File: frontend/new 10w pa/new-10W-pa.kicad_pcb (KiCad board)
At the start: 2 copper layers, 100 x 100 mm, 169 parts, among them K1 D3002, K2 D3002, K3 D3002, K4 D3002, K5 D3002, K6 D3002, P1 CONN_01X02, P2 CONN_02X01, P3 From HL CN3, P4 CONN_01X02, P5 CONN_01X02, P6 CONN_01X01, P7 From FE CN2, P8 CONN_01X08, P9 CONN_02X05, Q1 2N3906, Q3 RD16HHF1, T1 TRANSFO, T2 OUT_TRANSF, U1 74HC14, U2 74HC14, U3 TPIC6B595, U4 TPIC6B595, U5 TPIC6B595, U6 TPIC6B595, U7 LP2951-50D

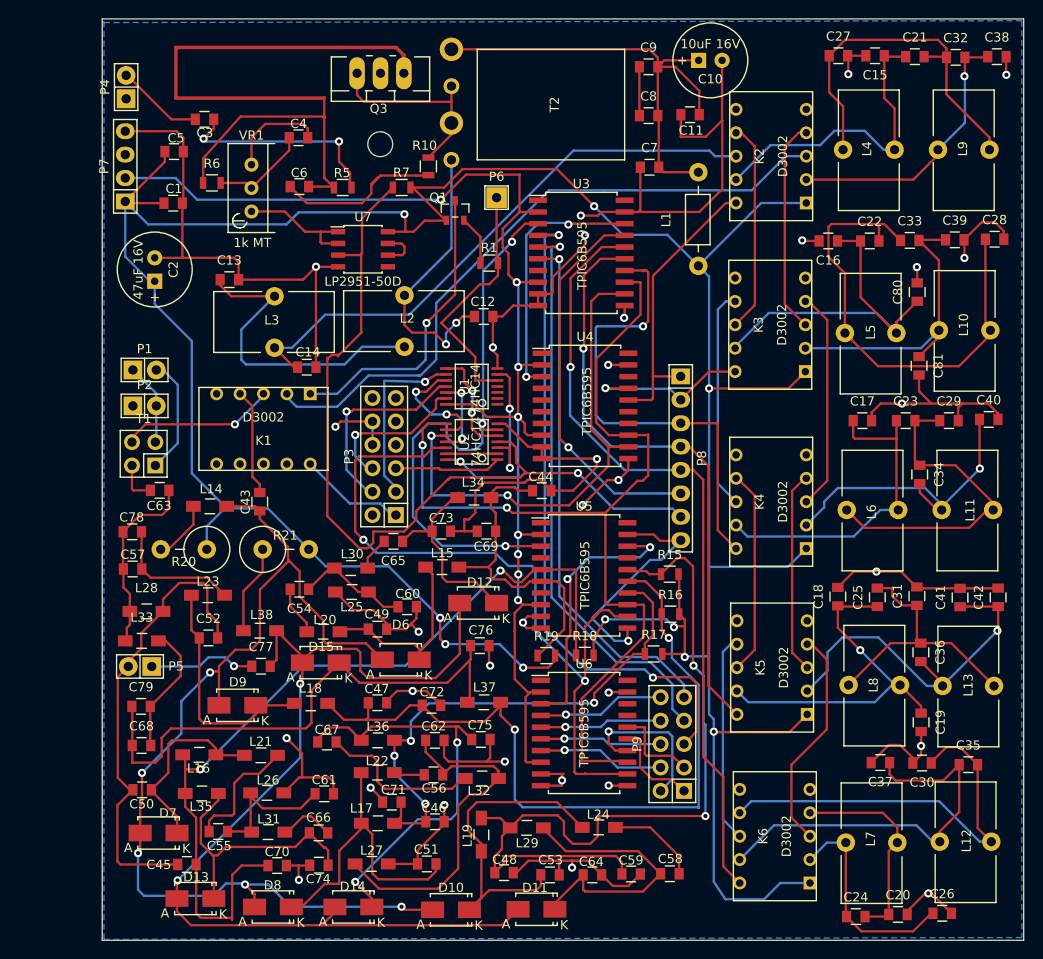
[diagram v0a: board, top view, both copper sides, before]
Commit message: new superband design and updated pcb
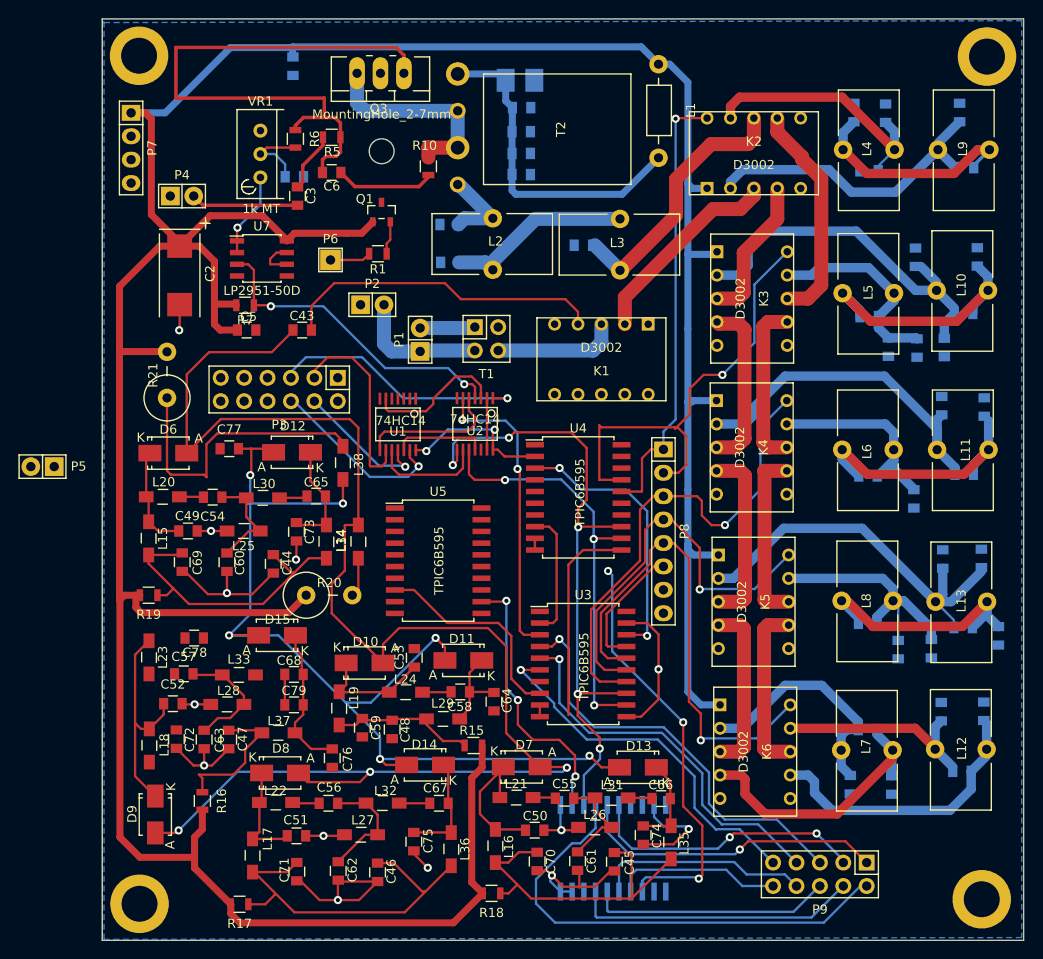
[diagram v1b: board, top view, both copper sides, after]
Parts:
- added MH: VAL**, HERMESLITE:MH, F.Cu at (196.0, 54.1)
- added MH: VAL**, HERMESLITE:MH, F.Cu at (195.5, 145.5)
- added MH: VAL**, HERMESLITE:MH, F.Cu at (104.0, 54.0)
- added MH: VAL**, HERMESLITE:MH, F.Cu at (104.1, 146.0)
- C1, C11, C12, C13, C14, C15, C16, C17, C18, C19, C20, C21, C22, C23, C24, C25, C26, C27, C28, C29, C30, C31, C32, C33, C34, C35, C36, C37, C38, C39, C4, C40, C41, C42, C7, C8, C80, C81, C9, U6: moved to B.Cu
- C10: footprint Discret:C1V8 -> Capacitors_Tantalum_SMD:TantalC_SizeB_EIA-3528_Reflow; moved to B.Cu
- C2: footprint Discret:C1V8 -> Capacitors_Tantalum_SMD:TantalC_SizeD_EIA-7343_Reflow
- moved R16 54.7 mm to (110.9, 134.9), turned to 270 degrees
- moved R17 52.5 mm to (114.9, 146.1), turned to 180 degrees
- moved L35 51.2 mm to (161.7, 139.4), turned to 270 degrees
- moved D13 50.1 mm to (158.1, 131.2)
- moved C45 46.4 mm to (155.6, 141.5), turned to 270 degrees
- moved U3 44.6 mm to (152.2, 120.0)
- moved R19 43.7 mm to (105.0, 112.5), turned to 180 degrees
- moved C50 42.8 mm to (146.9, 138.0), turned to 0 degrees
- moved D7 40.1 mm to (145.5, 131.2), turned to 180 degrees
- moved T1 39.2 mm to (141.7, 84.7), turned to 180 degrees
- moved L3 38.4 mm to (149.6, 77.8)
- moved C55 37.8 mm to (150.2, 134.6)
- moved K1 37.4 mm to (154.2, 86.9)
- moved L31 37.4 mm to (155.3, 134.5)
- moved C66 37.4 mm to (160.7, 134.6), turned to 180 degrees
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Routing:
- net GND: track 456.1 -> 132.0 mm, vias 33 -> 13
- net +5V: track 147.3 -> 54.0 mm, vias 9 -> 2
- net Net-(C48-Pad1): track 88.2 -> 15.6 mm, vias 2 -> 0
- net Net-(C47-Pad1): track 84.4 -> 15.3 mm, vias 2 -> 0
- net /PTT: track 94.1 -> 34.8 mm, vias 1 -> 2
- net Net-(C45-Pad1): track 92.9 -> 37.2 mm, vias 2 -> 0
- net RX-Load: track 81.5 -> 29.8 mm, vias 2 -> 3
- net Net-(C43-Pad1): track 112.6 -> 163.4 mm, vias 5 -> 3
- net TXOUT: track 72.0 -> 22.3 mm
- net Net-(C68-Pad1): track 58.7 -> 16.1 mm
- net SPI-CLK: track 106.2 -> 70.9 mm, vias 2 -> 5
- net Net-(P9-Pad2): track 17.3 -> 52.3 mm, vias 1 -> 0
- net Net-(C67-Pad1): track 46.7 -> 11.8 mm, vias 2 -> 0
- net +12V: track 338.3 -> 372.7 mm, vias 10 -> 0
- net TXIN: track 62.6 -> 29.1 mm
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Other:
- net class Power added: clearance 0.254, trace_width 0.762, via_dia 0.889, via_drill 0.635
- net class RF added: clearance 0.508, trace_width 1.524, via_dia 0.889, via_drill 0.635
- net class RF-N added: clearance 0.254, trace_width 1.016, via_dia 0.889, via_drill 0.635

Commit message: Board files updated
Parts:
- added MH: VAL**, HERMESLITE:MH, F.Cu at (146.2, 54.1)
- added MH: VAL**, HERMESLITE:MH, F.Cu at (104.0, 96.1)
- added MH: VAL**, HERMESLITE:MH, F.Cu at (146.1, 84.6)
- moved P5 20.6 mm to (103.0, 80.3), turned to 90 degrees
- moved P2 11.2 mm to (125.6, 70.4)
- moved C11 9.17 mm to (153.8, 63.1), turned to 90 degrees
- moved C10 7.27 mm to (143.7, 63.7), turned to 270 degrees
- moved C8 6.30 mm to (151.6, 63.0), turned to 90 degrees
- moved P1 5.78 mm to (130.6, 80.5)
- moved R17 5.52 mm to (113.1, 140.9)
- moved T1 5.09 mm to (137.2, 82.4)
- moved C9 3.91 mm to (149.3, 63.0), turned to 90 degrees
- moved C7 3.66 mm to (147.0, 63.0), turned to 90 degrees
- moved D6 2.56 mm to (109.7, 96.5), turned to 270 degrees
- moved K1 2.26 mm to (156.4, 87.3), turned to 270 degrees
- moved R21 1.42 mm to (106.2, 87.5)
- moved L36 0.65 mm to (137.3, 139.8)
- moved C62 0.05 mm to (125.6, 142.5)
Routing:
- net +5V: track 54.0 -> 224.1 mm, vias 2 -> 12
- net GND: track 132.0 -> 266.7 mm, vias 13 -> 32
- net Net-(C47-Pad1): track 15.3 -> 74.3 mm, vias 0 -> 2
- net Net-(C45-Pad1): track 37.2 -> 78.4 mm, vias 0 -> 2
- net /PTT: track 34.8 -> 74.4 mm, vias 2 -> 6
- net Net-(K1-Pad1): track 0.00 -> 31.0 mm
- net Net-(C46-Pad1): track 40.5 -> 67.7 mm, vias 0 -> 2
- net Net-(C48-Pad1): track 15.6 -> 41.5 mm, vias 0 -> 3
- net RX-OUT: track 0.00 -> 20.6 mm, vias 0 -> 2
- net SPI-DATA: track 32.9 -> 51.0 mm, vias 2 -> 4
- net Net-(P6-Pad1): track 4.47 -> 22.4 mm, vias 0 -> 1
- net RX-Load: track 29.8 -> 47.4 mm, vias 3 -> 4
- net Net-(U5-Pad18): track 45.4 -> 62.6 mm, vias 3 -> 5
- net Net-(P9-Pad2): track 52.3 -> 41.1 mm, vias 0 -> 1
- net SPI-CLK: track 70.9 -> 81.4 mm, vias 5 -> 6
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
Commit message: Upload latest pcb changes
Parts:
- removed MH (x7): VAL**, HERMESLITE:MH
- removed MountingHole_2-7mm: VAL**, Mounting_Holes:MountingHole_2-7mm
- added MountingHole_4mm: VAL**, Mounting_Holes:MountingHole_4mm, F.Cu at (104.4, 92.4)
- added MountingHole_4mm: VAL**, Mounting_Holes:MountingHole_4mm, F.Cu at (146.4, 84.1)
- added MountingHole_4mm: VAL**, Mounting_Holes:MountingHole_4mm, F.Cu at (146.6, 53.8)
- added MountingHole_4mm: VAL**, Mounting_Holes:MountingHole_4mm, F.Cu at (104.3, 54.3)
- added MountingHole_4mm: VAL**, Mounting_Holes:MountingHole_4mm, F.Cu at (104.2, 145.8)
- added MountingHole_4mm: VAL**, Mounting_Holes:MountingHole_4mm, F.Cu at (195.6, 145.7)
- added MountingHole_4mm: VAL**, Mounting_Holes:MountingHole_4mm, F.Cu at (195.6, 54.3)
- added MountingHole_6mm: VAL**, Mounting_Holes:MountingHole_6mm, F.Cu at (130.5, 66.9)
- U6: moved to F.Cu
- moved C45 47.9 mm to (115.9, 114.6), turned to 0 degrees
- moved C50 40.7 mm to (115.7, 112.0)
- moved C66 40.6 mm to (128.9, 109.4)
- moved C74 40.3 mm to (128.8, 111.6), turned to 180 degrees
- moved D7 40.0 mm to (108.6, 115.9), turned to 90 degrees
- moved L31 39.9 mm to (124.2, 109.5)
- moved L16 39.7 mm to (112.7, 113.8)
- moved C55 39.6 mm to (119.4, 109.6)
- moved C61 39.5 mm to (124.5, 112.6)
- moved L26 39.4 mm to (122.4, 113.6), turned to 270 degrees
- moved L35 39.3 mm to (132.1, 113.6)
- moved L21 39.3 mm to (114.5, 109.7)
- moved R18 36.4 mm to (119.7, 116.3), turned to 90 degrees
- moved R21 34.0 mm to (135.4, 104.8)
- moved C70 32.7 mm to (128.8, 114.4), turned to 180 degrees
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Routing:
- net GND: track 266.7 -> 146.3 mm, vias 32 -> 27
- net Net-(C43-Pad1): track 157.4 -> 41.0 mm, vias 3 -> 0
- net Net-(C77-Pad2): track 110.5 -> 44.9 mm, vias 6 -> 0
- net +12V: track 378.9 -> 318.4 mm, vias 1 -> 6
- net Net-(U5-Pad18): track 62.6 -> 12.0 mm, vias 5 -> 0
- net +5V: track 224.1 -> 181.7 mm, vias 12 -> 4
- net Net-(C47-Pad1): track 74.3 -> 41.7 mm
- net RX-OUT: track 20.6 -> 51.5 mm, vias 2 -> 0
- net RX-Load: track 47.4 -> 77.7 mm, vias 4 -> 3
- net Net-(C45-Pad1): track 78.4 -> 49.9 mm
- net SPI-CLK: track 81.4 -> 105.4 mm
- net Net-(C44-Pad1): track 42.9 -> 63.7 mm
- net Net-(L38-Pad1): track 26.5 -> 5.86 mm, vias 1 -> 0
- net RX-IN: track 39.2 -> 57.9 mm
- net Net-(C58-Pad1): track 10.0 -> 27.4 mm
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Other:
- net class Gnd added: clearance 0.254, trace_width 0.381, via_dia 0.889, via_drill 0.635

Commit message: More pcb changes
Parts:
- added C82: 0.1uF, HERMESLITE:C_0805, F.Cu at (165.0, 72.3)
- C1: moved to F.Cu
- moved C1 13.5 mm to (108.2, 60.2), turned to 0 degrees
- moved R10 13.4 mm to (134.1, 63.6), turned to 180 degrees
- moved C6 10.3 mm to (129.1, 62.4)
- moved R16 10.1 mm to (110.2, 134.3)
- moved R15 10.1 mm to (110.1, 145.1)
- moved Q1 8.20 mm to (123.6, 75.7)
- moved R18 6.50 mm to (113.7, 118.8), turned to 180 degrees
- moved C21 5.60 mm to (193.4, 61.6)
- moved R17 5.12 mm to (115.5, 129.3), turned to 180 degrees
- moved MountingHole_6mm 4.31 mm to (130.2, 71.2)
- moved R1 3.63 mm to (121.1, 80.2), turned to 270 degrees
- moved P2 3.00 mm to (124.9, 78.9)
- moved C12 1.11 mm to (138.7, 72.7)
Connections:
- C43 pad 2: RX-IN -> RX-OUT
- C77 pad 1: RX-OUT -> RX-IN
- K1 pad 2: TXOUT -> RX-IN
- K1 pad 4: RX-IN -> TXOUT
- K2 pad 2: Net-(C32-Pad2) -> Net-(K2-Pad2)
- K2 pad 4: Net-(K2-Pad4) -> Net-(C32-Pad2)
- K2 pad 7: Net-(K2-Pad7) -> Net-(C15-Pad1)
- K2 pad 8: TXIN -> Net-(C82-Pad1)
- K2 pad 9: Net-(C15-Pad1) -> Net-(K2-Pad9)
- K3 pad 2: Net-(C33-Pad2) -> Net-(K3-Pad2)
- K3 pad 3: Net-(K2-Pad4) -> Net-(K2-Pad2)
- K3 pad 4: Net-(K3-Pad4) -> Net-(C33-Pad2)
- K3 pad 7: Net-(K3-Pad7) -> Net-(C16-Pad1)
- K3 pad 8: Net-(K2-Pad7) -> Net-(K2-Pad9)
- K3 pad 9: Net-(C16-Pad1) -> Net-(K3-Pad9)
- K4 pad 2: Net-(C34-Pad2) -> Net-(K4-Pad2)
- K4 pad 3: Net-(K3-Pad4) -> Net-(K3-Pad2)
- K4 pad 4: Net-(K4-Pad4) -> Net-(C34-Pad2)
- K4 pad 7: Net-(K4-Pad7) -> Net-(C17-Pad1)
- K4 pad 8: Net-(K3-Pad7) -> Net-(K3-Pad9)
- K4 pad 9: Net-(C17-Pad1) -> Net-(K4-Pad9)
- K5 pad 2: Net-(C36-Pad2) -> Net-(K5-Pad2)
- K5 pad 3: Net-(K4-Pad4) -> Net-(K4-Pad2)
- K5 pad 4: Net-(K5-Pad4) -> Net-(C36-Pad2)
- K5 pad 7: Net-(K5-Pad7) -> Net-(C18-Pad1)
- K5 pad 8: Net-(K4-Pad7) -> Net-(K4-Pad9)
- K5 pad 9: Net-(C18-Pad1) -> Net-(K5-Pad9)
- K6 pad 2: Net-(C24-Pad1) -> Net-(C20-Pad1)
- K6 pad 3: Net-(K5-Pad4) -> Net-(K5-Pad2)
- K6 pad 4: Net-(C20-Pad1) -> Net-(C24-Pad1)
- K6 pad 7: Net-(C30-Pad1) -> Net-(C35-Pad1)
- K6 pad 8: Net-(K5-Pad7) -> Net-(K5-Pad9)
- K6 pad 9: Net-(C35-Pad1) -> Net-(C30-Pad1)
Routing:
- net +12V: track 318.4 -> 351.1 mm, vias 6 -> 12
- net GND: track 146.3 -> 115.3 mm, vias 27 -> 43
- net RX-IN: track 57.9 -> 28.1 mm, vias 1 -> 3
- net RX-OUT: track 51.5 -> 25.1 mm
- net Net-(C6-Pad1): track 27.3 -> 3.55 mm
- net Net-(K3-Pad2): track 0.00 -> 23.5 mm
- net Net-(K5-Pad9): track 0.00 -> 22.9 mm
- net Net-(K4-Pad9): track 0.00 -> 22.8 mm
- net Net-(K5-Pad2): track 0.00 -> 22.8 mm
- net Net-(K3-Pad9): track 0.00 -> 22.7 mm
- net Net-(K4-Pad2): track 0.00 -> 22.5 mm
- net Net-(K2-Pad9): track 0.00 -> 21.4 mm
- net Net-(K2-Pad2): track 0.00 -> 21.3 mm
- net Net-(K3-Pad7): track 18.5 -> 0.00 mm
- net Net-(K3-Pad4): track 18.4 -> 0.00 mm
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
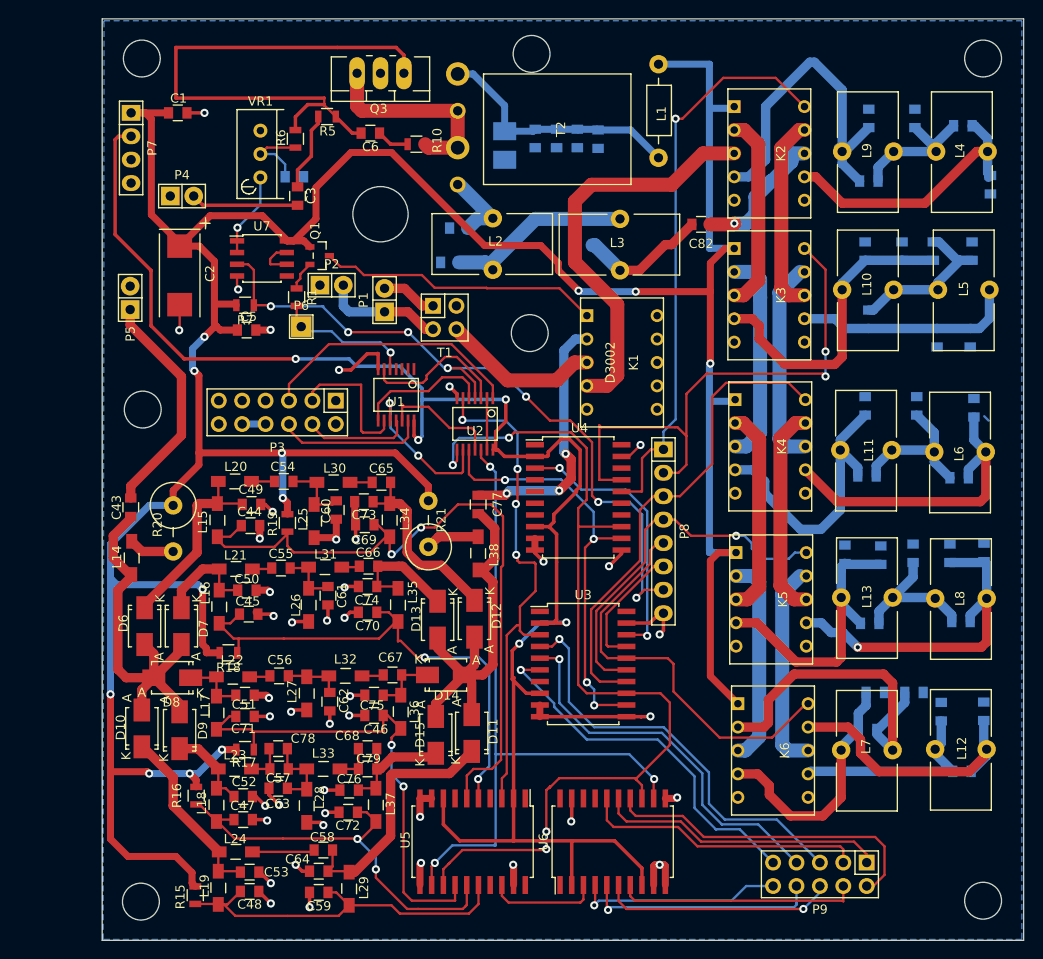
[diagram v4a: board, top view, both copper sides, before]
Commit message: Board edge added
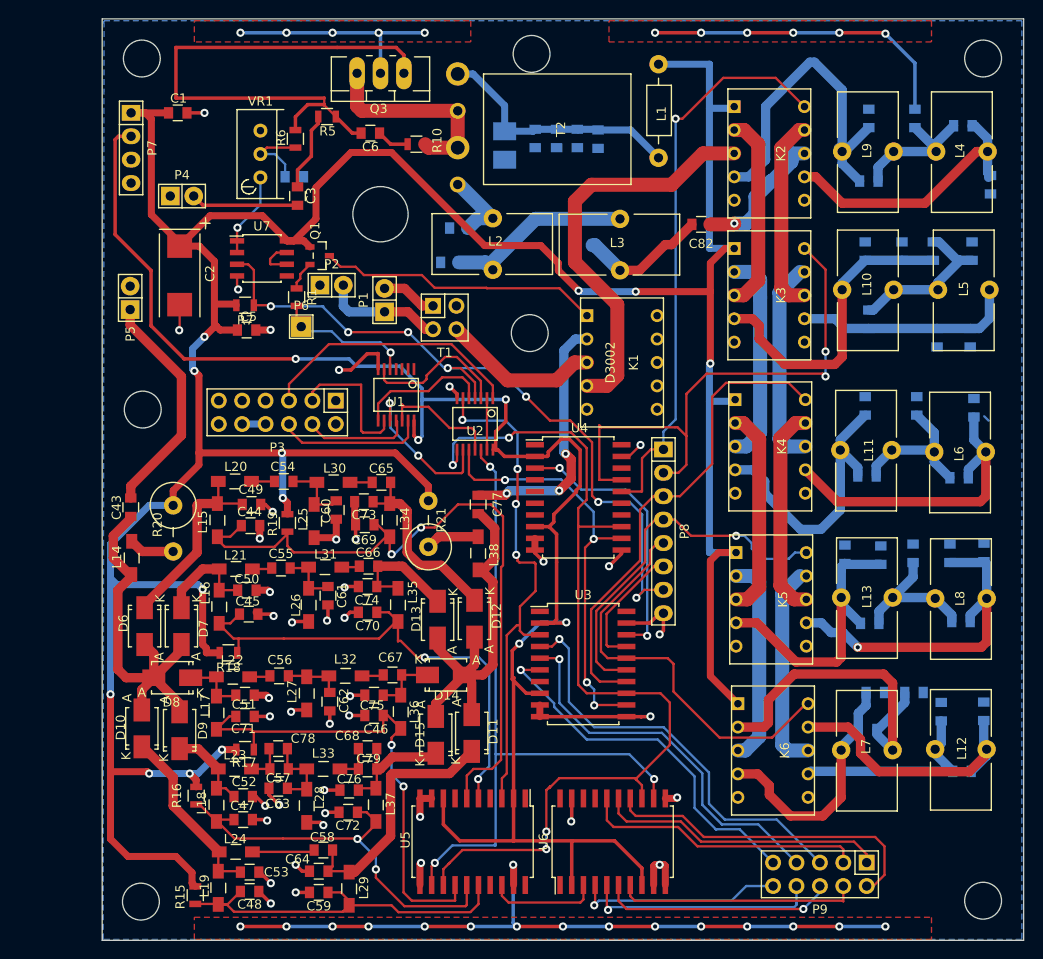
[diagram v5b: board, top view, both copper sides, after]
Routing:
- net GND: track 115.3 -> 251.3 mm, vias 43 -> 69
- added copper zone on F.Cu, net GND
